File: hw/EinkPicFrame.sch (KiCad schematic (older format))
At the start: 22 parts, among them J1 Conn_01x02_Male, J2 AVR-ISP-6, J3 Conn_01x06_Female, J4 Conn_01x08_Male, J5 Conn_01x03_Male, Q1 2N7000, Q2 2N7000, SW1 SW_Push, U1 ATmega328P-PU

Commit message: HW: Created PCB
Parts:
- added C3: CP, Capacitor_THT:CP_Radial_D6.3mm_P2.50mm, symbol Device:CP
- added D1: LED, LED_THT:LED_D4.0mm, symbol Device:LED
- added J6: TRIG, Connector_PinHeader_2.54mm:PinHeader_1x02_P2.54mm_Vertical, symbol Connector:Conn_01x02_Male
- added R11: 330, Resistor_THT:R_Axial_DIN0204_L3.6mm_D1.6mm_P2.54mm_Vertical, symbol Device:R
- J1: renamed from J3; value Conn_01x06_Female -> SD; footprint Connector_PinSocket_2.54mm:PinSocket_1x06_P2.54mm_Horizontal -> Connector_PinSocket_2.54mm:PinSocket_1x06_P2.54mm_Vertical
- J3: renamed from J4; value Conn_01x08_Male -> EPD; footprint Connector_PinHeader_2.54mm:PinHeader_2x04_P2.54mm_Horizontal -> Connector_PinHeader_2.54mm:PinHeader_2x04_P2.54mm_Vertical
- J4: renamed from J1; value Conn_01x02_Male -> Power
- J5: value Conn_01x03_Male -> UART; footprint Connector_PinHeader_2.54mm:PinHeader_1x03_P2.54mm_Horizontal -> Connector_PinSocket_2.54mm:PinSocket_1x03_P2.54mm_Vertical
- renumbered C3 to C4, R9 to R1, R5 to R10, R3 to R2, R10 to R3, R6 to R4, R7 to R5, R8 to R6, R1 to R7, R4 to R8, R2 to R9
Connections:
- net +3V3: now also J3.7 (Pin_7), R2.2, C3.1
- net DPCS: now also J3.6 (Pin_6); no longer J3.2 (Pin_2), J3.5 (Pin_5)
- net DPDC: now also J3.4 (Pin_4); no longer J3.6 (Pin_6)
- net DPRST: now also J3.5 (Pin_5); no longer J3.7 (Pin_7)
- net GND: now also C3.2, J6.1 (Pin_1), R11.1
- net RESET: now also SW1.2
- net SCK: now also J3.2 (Pin_2); no longer J3.4 (Pin_4)
- net LED: now reaches U1.4 (PD2)
- net LED: now also D1.2 (A)
- net TRIG: now reaches U1.5 (PD3)
- net TRIG: now also J6.2 (Pin_2)
- new net: D1.1 (K), R11.2
- no-connect marks 10 -> 8
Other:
- note added: "Debug"
- moved on the sheet: C1, C2, C4, J4, Q1, Q2, R10, R2, R3, R7, R8, R9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

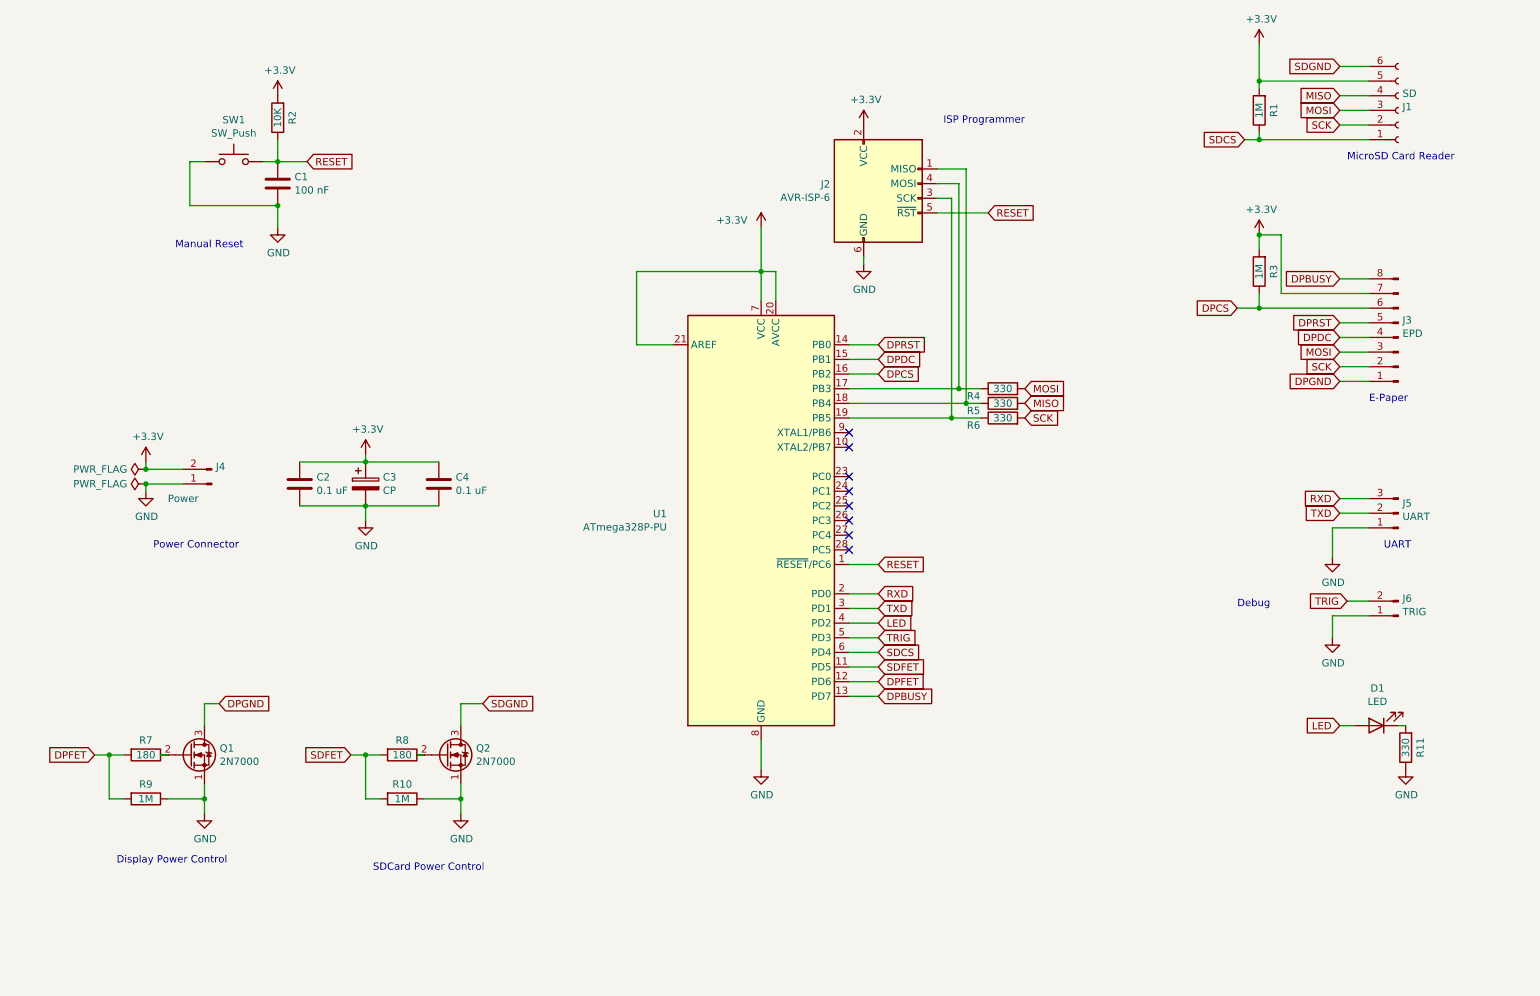
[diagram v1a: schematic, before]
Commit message: HW: Added possibility to add a crystal
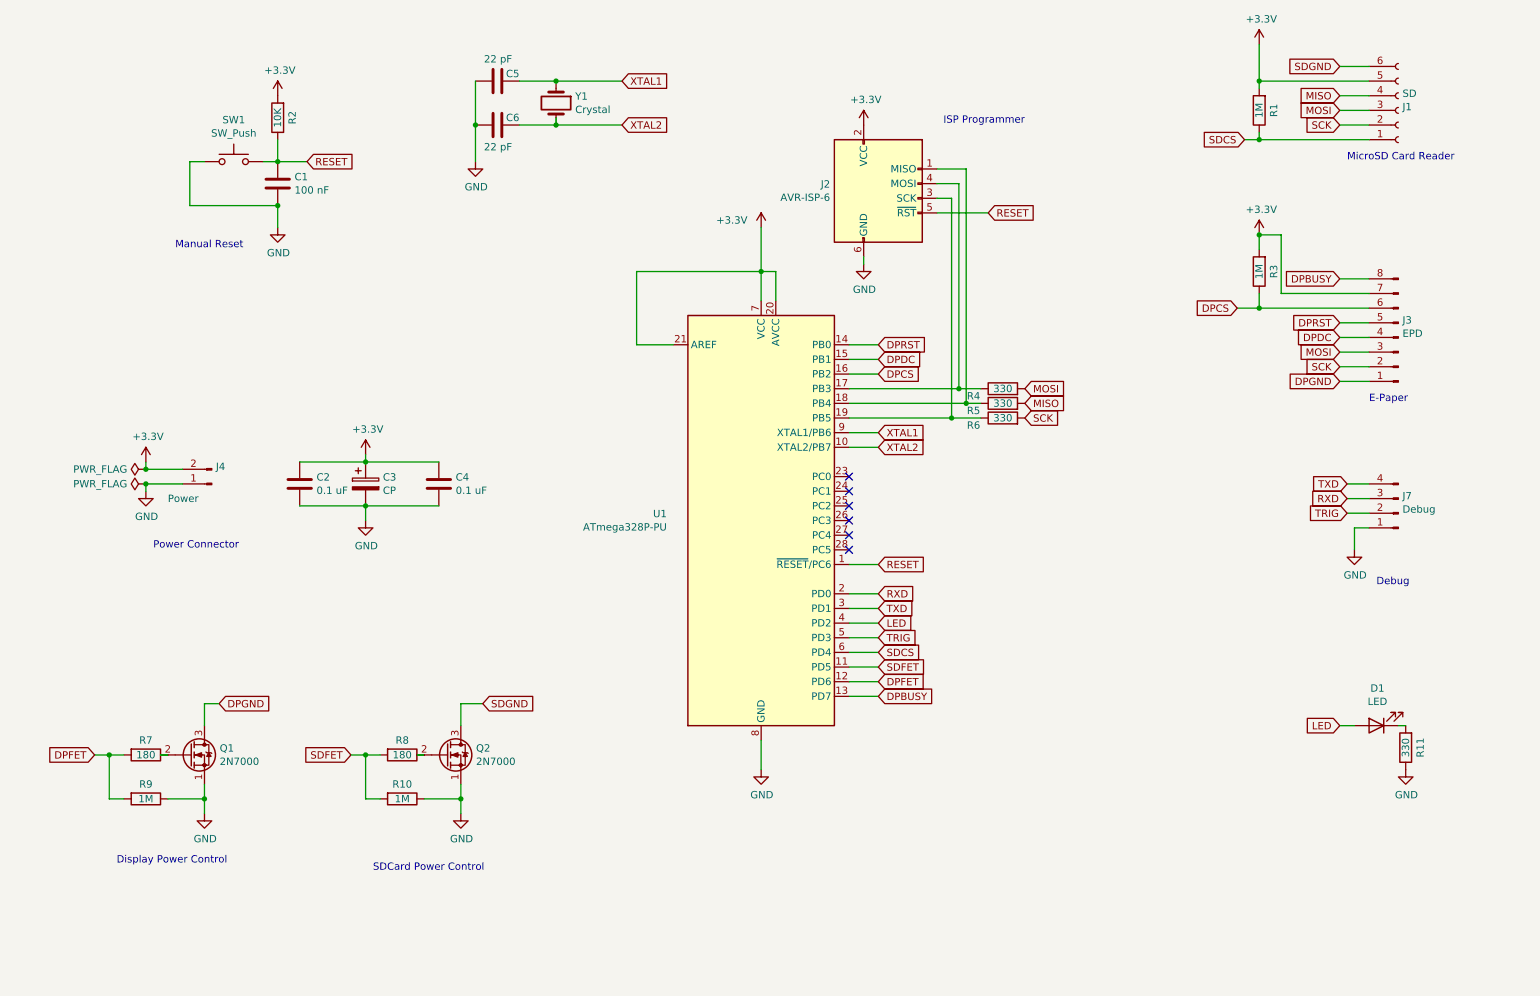
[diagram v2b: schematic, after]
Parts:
- removed J5: UART, Connector_PinSocket_2.54mm:PinSocket_1x03_P2.54mm_Vertical, symbol Connector:Conn_01x03_Male
- removed J6: TRIG, Connector_PinHeader_2.54mm:PinHeader_1x02_P2.54mm_Vertical, symbol Connector:Conn_01x02_Male
- added C5, C6: 22 pF, Capacitor_THT:C_Disc_D5.1mm_W3.2mm_P5.00mm, symbol Device:C
- added J7: Debug, Connector_PinHeader_2.54mm:PinHeader_1x04_P2.54mm_Vertical, symbol Connector:Conn_01x04_Male
- added Y1: Crystal, Crystal:Crystal_C38-LF_D3.0mm_L8.0mm_Vertical, symbol Device:Crystal
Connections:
- net GND: now also C5.1, C6.1, J7.1 (Pin_1)
- net RXD: now also J7.3 (Pin_3)
- net TRIG: now also J7.2 (Pin_2)
- net TXD: now also J7.4 (Pin_4)
- net XTAL2: now reaches U1.10 (XTAL2/PB7)
- net XTAL2: now also C6.2, Y1.2
- net XTAL1: now reaches U1.9 (XTAL1/PB6)
- net XTAL1: now also C5.2, Y1.1
- no-connect marks 8 -> 6
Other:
- note removed: "UART"
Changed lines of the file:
@@
 Wire Wire Line
 	4750 2650 5600 2650
-$Comp
-L Connector:Conn_01x03_Male J5
-U 1 1 61B48A02
-P 9950 4300
-F 0 "J5" H 9922 4232 50  0000 R CNN
-F 1 "UART" H 9922 4323 50  0000 R CNN
-F 2 "Connector_PinSocket_2.54mm:PinSocket_1x03_P2.54mm_Vertical" H 9950 4300 50  0001 C CNN
-F 3 "~" H 9950 4300 50  0001 C CNN
-	1    9950 4300
-	-1   0    0    1
-$EndComp
-Text Notes 9850 4550 0    50   ~ 0
-UART
-$Comp
-L power:GND #PWR012
-U 1 1 61B4B700
-P 9500 4600
-F 0 "#PWR012" H 9500 4350 50  0001 C CNN
-F 1 "GND" H 9505 4427 50  0000 C CNN
-F 2 "" H 9500 4600 50  0001 C CNN
-F 3 "" H 9500 4600 50  0001 C CNN
-	1    9500 4600
-	1    0    0    -1
-$EndComp
 Text GLabel 6400 4850 2    50   Input ~ 0
 RXD
@@
 Wire Wire Line
 	6200 4950 6400 4950
-Text GLabel 9550 4200 0    50   Input ~ 0
+Text GLabel 9600 4200 0    50   Input ~ 0
 RXD
-Text GLabel 9550 4300 0    50   Input ~ 0
+Text GLabel 9600 4100 0    50   Input ~ 0
 TXD
-Wire Wire Line
-	9550 4200 9750 4200
-Wire Wire Line
-	9550 4300 9750 4300
 Text GLabel 6400 5250 2    50   Input ~ 0
 SDCS
@@
 Text Notes 1450 4550 0    50   ~ 0
 Power Connector\n
-NoConn ~ 6200 3850
 NoConn ~ 6200 4050
 NoConn ~ 6200 4150
@@
 	2900 3900 2900 3950
 Connection ~ 2900 3950
-NoConn ~ 6200 3750
 Wire Wire Line
 	9000 1100 9000 1350
@@
 Wire Wire Line
 	6200 5050 6400 5050
-Text GLabel 9600 4900 0    50   Input ~ 0
+Text GLabel 9600 4300 0    50   Input ~ 0
 TRIG
-Wire Wire Line
-	9600 4900 9750 4900
-Wire Wire Line
-	9500 4600 9500 4400
-Wire Wire Line
-	9500 4400 9750 4400
-$Comp
-L Connector:Conn_01x02_Male J6
-U 1 1 61D5C6CC
-P 9950 5000
-F 0 "J6" H 9922 4882 50  0000 R CNN
-F 1 "TRIG" H 9922 4973 50  0000 R CNN
-F 2 "Connector_PinHeader_2.54mm:PinHeader_1x02_P2.54mm_Vertical" H 9950 5000 50  0001 C CNN
-F 3 "~" H 9950 5000 50  0001 C CNN
-	1    9950 5000
-	-1   0    0    1
-$EndComp
 $Comp
 L power:GND #PWR013
 U 1 1 61D611B9
-P 9500 5150
-F 0 "#PWR013" H 9500 4900 50  0001 C CNN
-F 1 "GND" H 9505 4977 50  0000 C CNN
-F 2 "" H 9500 5150 50  0001 C CNN
-F 3 "" H 9500 5150 50  0001 C CNN
-	1    9500 5150
-	1    0    0    -1
-$EndComp
-Wire Wire Line
-	9500 5150 9500 5000
-Wire Wire Line
-	9500 5000 9750 5000
-Text Notes 8850 4950 0    50   ~ 0
+P 9650 4550
+F 0 "#PWR013" H 9650 4300 50  0001 C CNN
+F 1 "GND" H 9655 4377 50  0000 C CNN
+F 2 "" H 9650 4550 50  0001 C CNN
+F 3 "" H 9650 4550 50  0001 C CNN
+	1    9650 4550
+	1    0    0    -1
+$EndComp
+Text Notes 9800 4800 0    50   ~ 0
 Debug
 $Comp
@@
 Wire Wire Line
 	9550 3100 9750 3100
+$Comp
+L Device:Crystal Y1
+U 1 1 61D346AE
+P 4200 1500
+F 0 "Y1" V 4154 1631 50  0000 L CNN
+F 1 "Crystal" V 4245 1631 50  0000 L CNN
+F 2 "Crystal:Crystal_C38-LF_D3.0mm_L8.0mm_Vertical" H 4200 1500 50  0001 C CNN
+F 3 "~" H 4200 1500 50  0001 C CNN
+	1    4200 1500
+	0    1    1    0
+$EndComp
+Text GLabel 6400 3750 2    50   Input ~ 0
+XTAL1
+Text GLabel 6400 3850 2    50   Input ~ 0
+XTAL2
+Wire Wire Line
+	6200 3750 6400 3750
+Wire Wire Line
+	6200 3850 6400 3850
+$Comp
+L Device:C C6
+U 1 1 61D60382
+P 3800 1650
+F 0 "C6" V 3850 1500 50  0000 L CNN
+F 1 "22 pF" V 3650 1550 50  0000 L CNN
+F 2 "Capacitor_THT:C_Disc_D5.1mm_W3.2mm_P5.00mm" H 3838 1500 50  0001 C CNN
+F 3 "~" H 3800 1650 50  0001 C CNN
+	1    3800 1650
+	0    -1   -1   0
+$EndComp
+$Comp
+L Device:C C5
+U 1 1 61D61050
+P 3800 1350
+F 0 "C5" V 3850 1200 50  0000 L CNN
+F 1 "22 pF" V 3950 1250 50  0000 L CNN
+F 2 "Capacitor_THT:C_Disc_D5.1mm_W3.2mm_P5.00mm" H 3838 1200 50  0001 C CNN
+F 3 "~" H 3800 1350 50  0001 C CNN
+	1    3800 1350
+	0    -1   -1   0
+$EndComp
+Wire Wire Line
+	3950 1350 4200 1350
+$Comp
+L power:GND #PWR018
+U 1 1 61D698A6
+P 3650 1900
+F 0 "#PWR018" H 3650 1650 50  0001 C CNN
+F 1 "GND" H 3655 1727 50  0000 C CNN
+F 2 "" H 3650 1900 50  0001 C CNN
+F 3 "" H 3650 1900 50  0001 C CNN
+	1    3650 1900
+	1    0    0    -1
+$EndComp
+Wire Wire Line
+	3650 1350 3650 1650
+Wire Wire Line
+	3650 1900 3650 1650
+Connection ~ 3650 1650
+Text GLabel 4650 1350 2    50   Input ~ 0
+XTAL1
+Text GLabel 4650 1650 2    50   Input ~ 0
+XTAL2
+Wire Wire Line
+	4200 1350 4650 1350
+Connection ~ 4200 1350
+Wire Wire Line
+	4200 1600 4200 1650
+Connection ~ 4200 1650
+Wire Wire Line
+	4200 1650 4650 1650
+Wire Wire Line
+	3950 1650 4200 1650
+$Comp
+L Connector:Conn_01x04_Male J7
+U 1 1 61DA63F9
+P 9950 4300
+F 0 "J7" H 9922 4182 50  0000 R CNN
+F 1 "Debug" H 9922 4273 50  0000 R CNN
+F 2 "Connector_PinHeader_2.54mm:PinHeader_1x04_P2.54mm_Vertical" H 9950 4300 50  0001 C CNN
+F 3 "~" H 9950 4300 50  0001 C CNN
+	1    9950 4300
+	-1   0    0    1
+$EndComp
+Wire Wire Line
+	9600 4300 9750 4300
+Wire Wire Line
+	9650 4550 9650 4400
+Wire Wire Line
+	9650 4400 9750 4400
+Wire Wire Line
+	9600 4100 9750 4100
+Wire Wire Line
+	9600 4200 9750 4200
 $EndSCHEMATC

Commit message: HW: ADC + Small improvements (V1.1)
Added proper wiring for AVCC and AREF according to data sheet
 * 100 nF capacitor to ground on AREF
 *  10 uH inductor on AVCC

 Added header for unused PortC pins
  * May be used as 2nd SPI (bit bang)
  * Independent SPI would allow to power EPD and SD independently

Use larger footprint for the FET transistors for easier soldering

Add a jumper to disconnect VCC without pulling battery connector
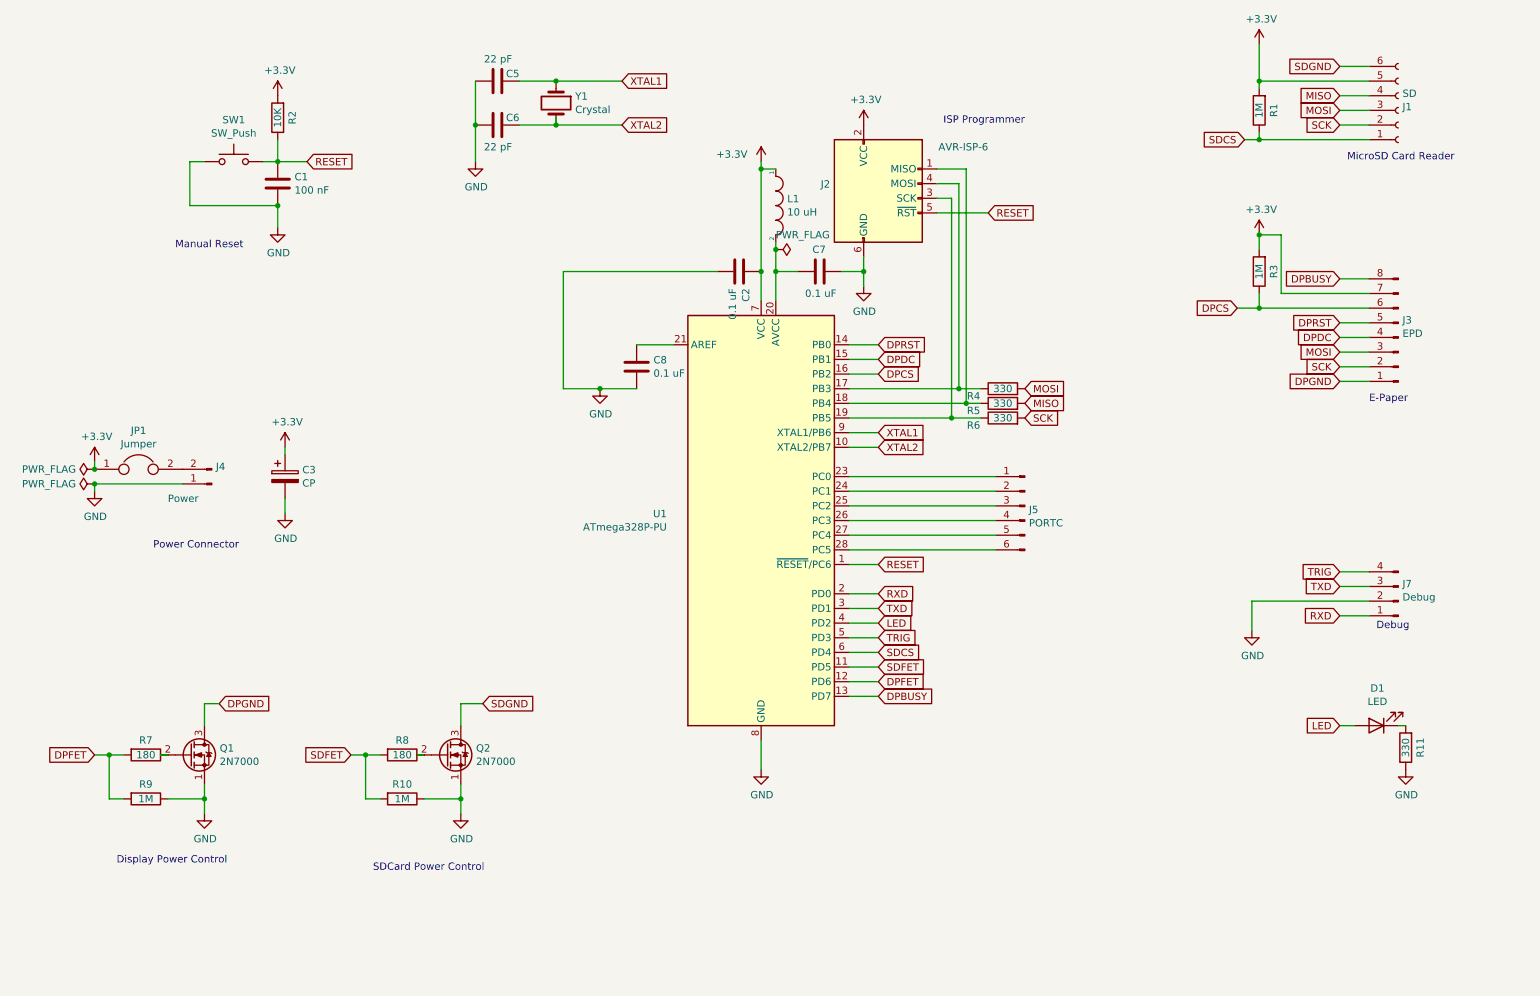
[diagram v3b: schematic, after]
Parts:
- removed C4: 0.1 uF, Capacitor_THT:C_Disc_D5.1mm_W3.2mm_P5.00mm, symbol Device:C
- added C7, C8: 0.1 uF, Capacitor_THT:C_Disc_D5.1mm_W3.2mm_P5.00mm, symbol Device:C
- added J5: PORTC, Connector_PinSocket_2.54mm:PinSocket_1x06_P2.54mm_Vertical, symbol Connector:Conn_01x06_Male
- added JP1: Jumper, Connector_PinHeader_2.54mm:PinHeader_1x02_P2.54mm_Vertical, symbol Device:Jumper
- added L1: 10 uH, Resistor_THT:R_Axial_DIN0204_L3.6mm_D1.6mm_P2.54mm_Vertical, symbol pspice:INDUCTOR
- J7: footprint Connector_PinHeader_2.54mm:PinHeader_1x04_P2.54mm_Vertical -> Connector_PinSocket_2.54mm:PinSocket_1x04_P2.54mm_Vertical
- Q1: footprint Package_TO_SOT_THT:TO-92_Inline -> Package_TO_SOT_THT:TO-92L_Inline_Wide
- Q2: footprint Package_TO_SOT_THT:TO-92_Inline -> Package_TO_SOT_THT:TO-92_Inline_Wide
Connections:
- net +3V3: now also JP1.1, L1.1; no longer J4.2 (Pin_2), U1.20 (AVCC), U1.21 (AREF)
- net GND: now also J7.2 (Pin_2), C7.1, C8.2; no longer J7.1 (Pin_1)
- net RXD: now also J7.1 (Pin_1); no longer J7.3 (Pin_3)
- net TRIG: now also J7.4 (Pin_4); no longer J7.2 (Pin_2)
- net TXD: now also J7.3 (Pin_3); no longer J7.4 (Pin_4)
- net at U1.23 (PC0): now also J5.1 (Pin_1)
- net at U1.24 (PC1): now also J5.2 (Pin_2)
- net at U1.25 (PC2): now also J5.3 (Pin_3)
- net at U1.26 (PC3): now also J5.4 (Pin_4)
- net at U1.27 (PC4): now also J5.5 (Pin_5)
- net at U1.28 (PC5): now also J5.6 (Pin_6)
- new net: C7.2, L1.2, U1.20 (AVCC)
- new net: C8.1, U1.21 (AREF)
- new net: J4.2 (Pin_2), JP1.2
- no-connect marks 6 -> 0
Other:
- moved on the sheet: C2, C3, J7
